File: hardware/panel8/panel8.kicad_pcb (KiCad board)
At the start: 2 copper layers, 99 x 67 mm, 200 parts, among them J1 Conn_01x02_Male, J2 Conn_01x08_Male, J3 Conn_01x02, J5 Conn_01x02_Male, J6 Conn_01x02_Male, J7 Conn_01x02_Male, U1 A7105-MODULE, U2 AIC1734-33GUTR, U3 ATtiny1617-M, U5 DRV8837DSGR, U6 DRV8837DSGR, U7 DRV8837DSGR

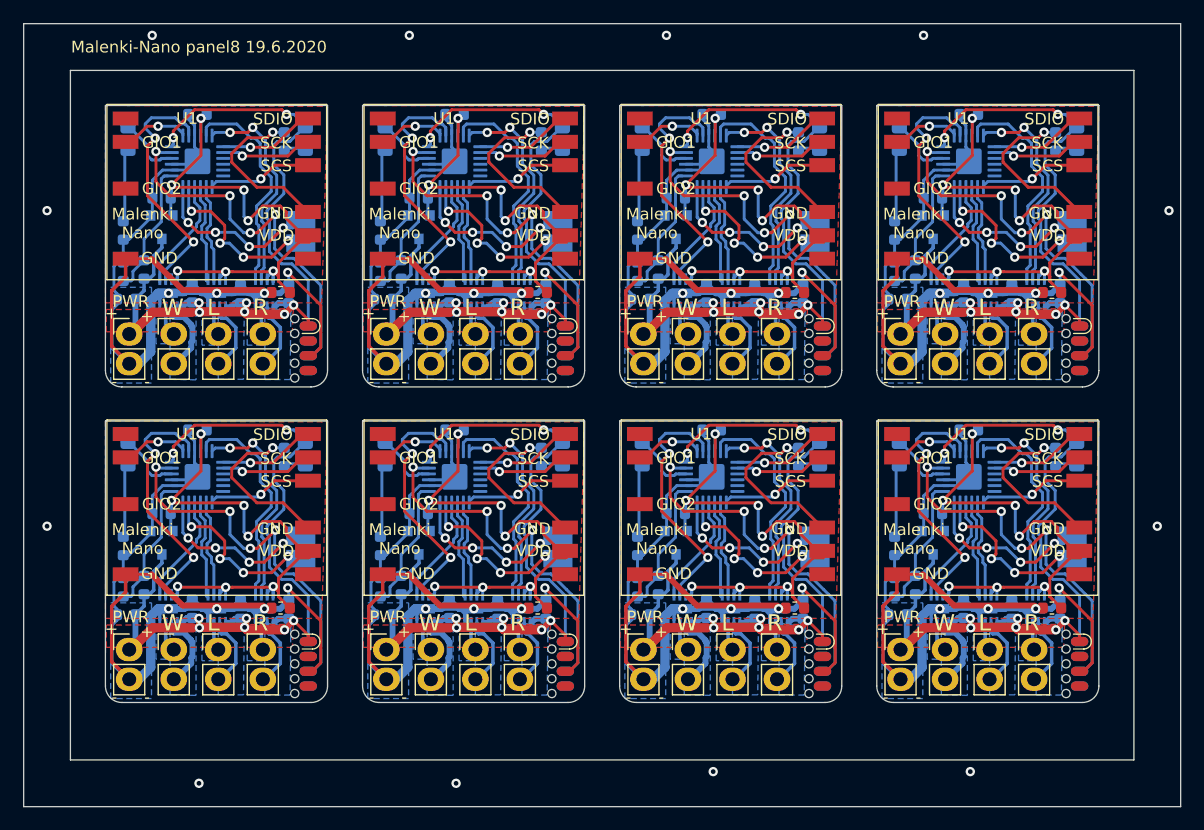
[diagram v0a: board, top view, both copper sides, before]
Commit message: Panel of 8
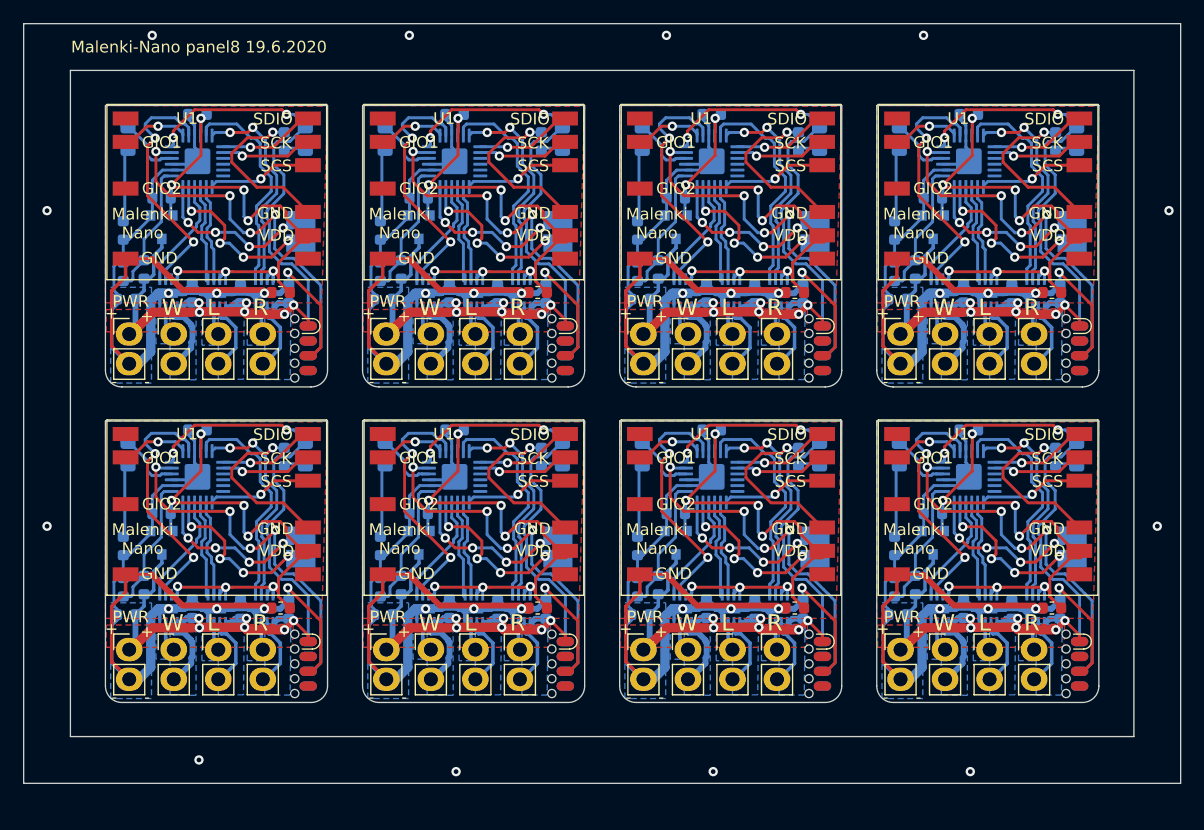
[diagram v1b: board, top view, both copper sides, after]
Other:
- board size 99 x 67 mm -> 99 x 65 mm
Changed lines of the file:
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@@
-(kicad_pcb (version 20200518) (host pcbnew "5.99.0-unknown-60915fb~101~ubuntu18.04.1")
+(kicad_pcb (version 20200625) (host pcbnew "5.99.0-unknown-af8f05d~101~ubuntu18.04.1")
   (general
     (thickness 1.6)
@@
     (pad_to_mask_clearance 0.051)
     (solder_mask_min_width 0.15)
-    (aux_axis_origin 0 0)
     (visible_elements FFFDF77F)
     (pcbplotparams
@@
     )
   )
-  (gr_line (start 125 134) (end 125 138) (layer "Eco2.User") (width 0.15))
+  (gr_line (start 125 132) (end 125 136) (layer "Eco2.User") (width 0.15))
   (gr_line (start 169 71) (end 169 75) (layer "Eco2.User") (width 0.15))
-  (gr_line (start 169 134) (end 169 138) (layer "Eco2.User") (width 0.15))
-  (gr_line (start 144 134) (end 144 138) (layer "Eco2.User") (width 0.15))
+  (gr_line (start 169 132) (end 169 136) (layer "Eco2.User") (width 0.15))
+  (gr_line (start 144 132) (end 144 136) (layer "Eco2.User") (width 0.15))
   (gr_line (start 125 71) (end 125 75) (layer "Eco2.User") (width 0.15))
   (gr_line (start 144 71) (end 144 75) (layer "Eco2.User") (width 0.15))
   (gr_line (start 191 71) (end 191 75) (layer "Eco2.User") (width 0.15))
-  (gr_line (start 191 134) (end 191 138) (layer "Eco2.User") (width 0.15))
+  (gr_line (start 191 132) (end 191 136) (layer "Eco2.User") (width 0.15))
   (gr_line (start 210 71) (end 210 75) (layer "Eco2.User") (width 0.15))
-  (gr_line (start 210 134) (end 210 138) (layer "Eco2.User") (width 0.15))
+  (gr_line (start 210 132) (end 210 136) (layer "Eco2.User") (width 0.15))
   (gr_text "Malenki-Nano panel8 19.6.2020" (at 133 73) (layer "F.SilkS")
     (effects (font (size 1 1) (thickness 0.15)))
@@
   )
   (gr_line (start 118 71) (end 217 71) (layer "Edge.Cuts") (width 0.05))
-  (gr_line (start 217 138) (end 118 138) (layer "Edge.Cuts") (width 0.05))
+  (gr_line (start 217 136) (end 118 136) (layer "Edge.Cuts") (width 0.05))
   (dimension 115 (width 0.15) (layer "Dwgs.User")
     (gr_text "115.000 mm" (at 179.5 155.3) (layer "Dwgs.User")
@@
     (arrow2b (pts (xy 122 154) (xy 123.126504 153.413579)))
   )
-  (gr_line (start 133 136) (end 133 129) (layer "Eco1.User") (width 0.15))
+  (gr_line (start 133 134) (end 133 127) (layer "Eco1.User") (width 0.15))
   (gr_line (start 120 114) (end 128 114) (layer "Eco1.User") (width 0.15))
-  (gr_line (start 155 136) (end 155 129) (layer "Eco1.User") (width 0.15))
+  (gr_line (start 155 135) (end 155 128) (layer "Eco1.User") (width 0.15))
   (dimension 4 (width 0.15) (layer "Dwgs.User")
     (gr_text "4.000 mm" (at 120 101.7) (layer "Dwgs.User")
@@
   )
   (gr_line (start 122 75) (end 213 75) (layer "Edge.Cuts") (width 0.05))
-  (gr_line (start 118 138) (end 118 71) (layer "Edge.Cuts") (width 0.05))
-  (gr_line (start 217 71) (end 217 138) (layer "Edge.Cuts") (width 0.05))
-  (gr_line (start 122 75) (end 122 134) (layer "Edge.Cuts") (width 0.05))
-  (gr_line (start 213 134) (end 122 134) (layer "Edge.Cuts") (width 0.05))
-  (gr_line (start 213 75) (end 213 134) (layer "Edge.Cuts") (width 0.05))
+  (gr_line (start 118 136) (end 118 71) (layer "Edge.Cuts") (width 0.05))
+  (gr_line (start 217 71) (end 217 136) (layer "Edge.Cuts") (width 0.05))
+  (gr_line (start 122 75) (end 122 132) (layer "Edge.Cuts") (width 0.05))
+  (gr_line (start 213 132) (end 122 132) (layer "Edge.Cuts") (width 0.05))
+  (gr_line (start 213 75) (end 213 132) (layer "Edge.Cuts") (width 0.05))
   (gr_circle (center 140.002 95.878) (end 140.129 95.878) (layer "B.SilkS") (width 0.5))
   (gr_circle (center 136.002 95.878) (end 136.129 95.878) (layer "B.SilkS") (width 0.5))
@@
   (via (at 153.173048 92.146952) (size 0.8) (drill 0.4) (layers "F.Cu" "B.Cu") (net 31))
   (via (at 120 114) (size 0.8) (drill 0.4) (layers "F.Cu" "B.Cu") (net 0))
-  (via (at 133 136) (size 0.8) (drill 0.4) (layers "F.Cu" "B.Cu") (net 0))
-  (via (at 155 136) (size 0.8) (drill 0.4) (layers "F.Cu" "B.Cu") (net 0))
+  (via (at 133 134) (size 0.8) (drill 0.4) (layers "F.Cu" "B.Cu") (net 0))
+  (via (at 155 135) (size 0.8) (drill 0.4) (layers "F.Cu" "B.Cu") (net 0))
   (segment (start 126.725 92.655) (end 125.531999 93.848001) (width 0.3) (layer "F.Cu") (net 1))
   (segment (start 126.725 91.112) (end 126.725 92.655) (width 0.3) (layer "F.Cu") (net 1))
